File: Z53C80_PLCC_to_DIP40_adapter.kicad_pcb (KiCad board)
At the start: 4 copper layers, 21.8 x 51.1 mm, 2 parts, among them J1 DIP40, J2 PLCC44

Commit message: Update PCB
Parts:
- added C1: 100nF, Capacitor_SMD:C_1206_3216Metric_Pad1.33x1.80mm_HandSolder, B.Cu at (105.9, 81.5)
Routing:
- net GND: track 0.00 -> 145.7 mm, vias 0 -> 35
- net /~{DB3}: track 0.00 -> 33.9 mm
- net /~{DB6}: track 0.00 -> 31.9 mm
- net /~{DB7}: track 0.00 -> 31.9 mm
- net /~{CS}: track 0.00 -> 30.7 mm
- net /~{MSG}: track 0.00 -> 28.5 mm
- net /C/~{D}: track 0.00 -> 25.9 mm
- net /~{DB5}: track 0.00 -> 25.8 mm
- net /~{REQ}: track 0.00 -> 25.6 mm
- net /~{IOR}: track 0.00 -> 23.4 mm
- net /~{DB4}: track 0.00 -> 23.4 mm
- net /I/~{O}: track 0.00 -> 20.5 mm
- net /~{DB2}: track 0.00 -> 18.3 mm
- net /IRQ: track 0.00 -> 18.3 mm
- net /DRQ: track 0.00 -> 18.0 mm
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- added copper zone on B.Cu, net GND
- added copper zone on F.Cu, net GND
- added copper zone on In1.Cu, net GND
- added copper zone on In2.Cu, net GND

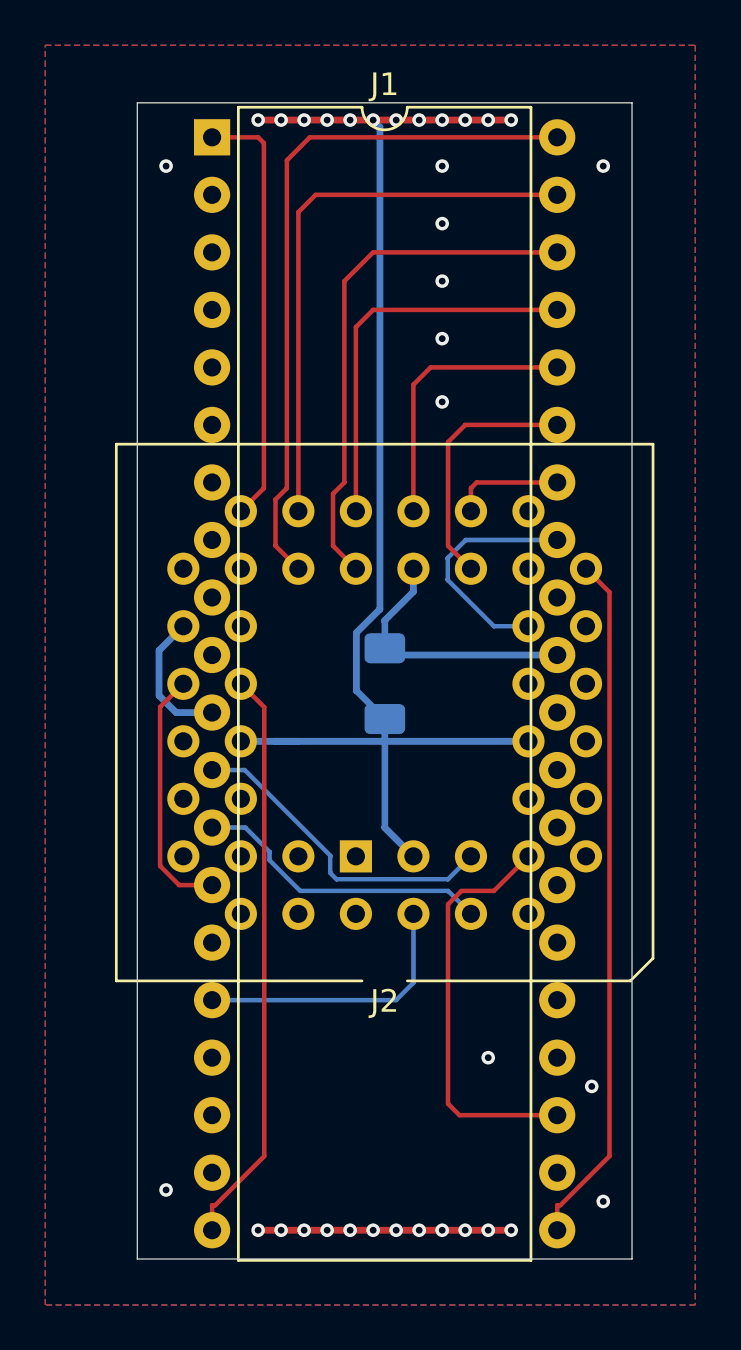
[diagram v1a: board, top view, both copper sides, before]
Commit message: Some more trace reorg
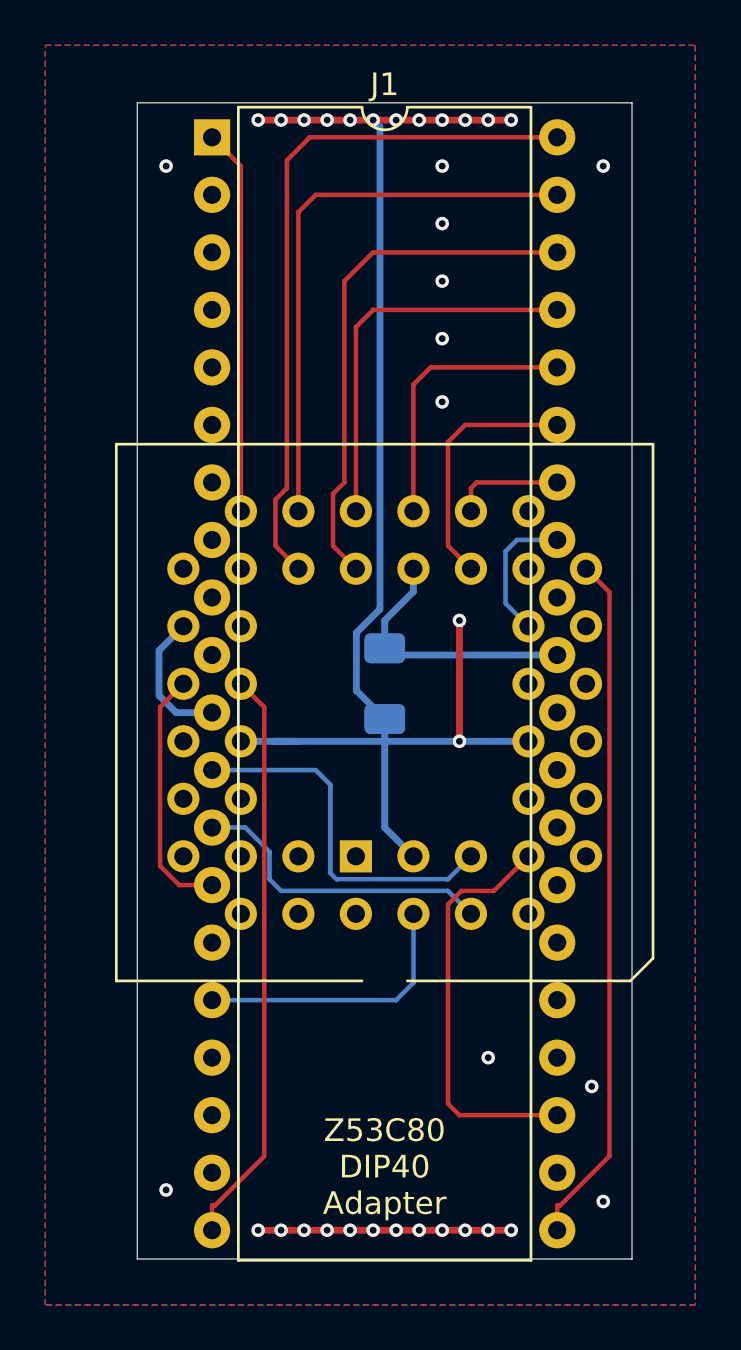
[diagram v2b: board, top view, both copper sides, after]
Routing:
- net GND: track 145.7 -> 151.0 mm, vias 35 -> 37
- net /A2: track 10.6 -> 6.22 mm
- net /D0: track 19.1 -> 17.0 mm
- net /~{SEL}: track 14.3 -> 16.1 mm
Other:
- board text added: "Z53C80 DIP40 Adapter"
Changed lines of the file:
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@@
 			(at -1.27 -6.4 0)
 			(layer "F.SilkS")
+			(hide yes)
 			(effects
 				(font
@@
 		(layer "Edge.Cuts")
 	)
-	(segment
-		(start 108.6996 75.9806)
-		(end 108.6996 76.9516)
+	(gr_text "Z53C80\nDIP40\nAdapter"
+		(at 105.918 102.87 0)
+		(layer "F.SilkS")
+		(effects
+			(font
+				(size 1 1)
+				(thickness 0.1)
+			)
+		)
+	)
+	(segment
+		(start 113.538 75.184)
+		(end 111.76 75.184)
 		(width 0.2)
 		(layer "B.Cu")
@@
 	)
 	(segment
-		(start 109.4962 75.184)
-		(end 108.6996 75.9806)
+		(start 111.2568 75.6872)
+		(end 111.76 75.184)
 		(width 0.2)
 		(layer "B.Cu")
@@
 	)
 	(segment
-		(start 108.6996 76.9516)
-		(end 110.742 78.994)
+		(start 111.2568 77.9828)
+		(end 111.2568 75.6872)
 		(width 0.2)
 		(layer "B.Cu")
@@
 	)
 	(segment
-		(start 110.742 78.994)
-		(end 112.268 78.994)
-		(width 0.2)
-		(layer "B.Cu")
-		(net 1)
-	)
-	(segment
-		(start 113.538 75.184)
-		(end 109.4962 75.184)
+		(start 112.268 78.994)
+		(end 111.2568 77.9828)
 		(width 0.2)
 		(layer "B.Cu")
@@
 	)
 	(segment
+		(start 100.838 88.9574)
+		(end 100.838 90.17)
+		(width 0.2)
+		(layer "B.Cu")
+		(net 10)
+	)
+	(segment
+		(start 99.7646 87.884)
+		(end 100.838 88.9574)
+		(width 0.2)
+		(layer "B.Cu")
+		(net 10)
+	)
+	(segment
 		(start 108.7131 90.6791)
-		(end 102.1894 90.6791)
+		(end 109.728 91.694)
 		(width 0.2)
 		(layer "B.Cu")
@@
 	)
 	(segment
-		(start 109.728 91.694)
+		(start 98.298 87.884)
+		(end 99.7646 87.884)
+		(width 0.2)
+		(layer "B.Cu")
+		(net 10)
+	)
+	(segment
+		(start 100.838 90.17)
+		(end 101.3471 90.6791)
+		(width 0.2)
+		(layer "B.Cu")
+		(net 10)
+	)
+	(segment
+		(start 101.3471 90.6791)
 		(end 108.7131 90.6791)
-		(width 0.2)
-		(layer "B.Cu")
-		(net 10)
-	)
-	(segment
-		(start 100.838 88.9574)
-		(end 99.7646 87.884)
-		(width 0.2)
-		(layer "B.Cu")
-		(net 10)
-	)
-	(segment
-		(start 102.1894 90.6791)
-		(end 100.838 89.3277)
-		(width 0.2)
-		(layer "B.Cu")
-		(net 10)
-	)
-	(segment
-		(start 100.838 89.3277)
-		(end 100.838 88.9574)
-		(width 0.2)
-		(layer "B.Cu")
-		(net 10)
-	)
-	(segment
-		(start 99.7646 87.884)
-		(end 98.298 87.884)
 		(width 0.2)
 		(layer "B.Cu")
@@
 	)
 	(segment
+		(start 102.87 85.344)
+		(end 98.298 85.344)
+		(width 0.2)
+		(layer "B.Cu")
+		(net 14)
+	)
+	(segment
+		(start 108.7151 90.1669)
+		(end 103.7956 90.1669)
+		(width 0.2)
+		(layer "B.Cu")
+		(net 14)
+	)
+	(segment
+		(start 103.5196 85.9936)
+		(end 102.87 85.344)
+		(width 0.2)
+		(layer "B.Cu")
+		(net 14)
+	)
+	(segment
+		(start 103.5196 89.8909)
+		(end 103.5196 85.9936)
+		(width 0.2)
+		(layer "B.Cu")
+		(net 14)
+	)
+	(segment
 		(start 103.7956 90.1669)
 		(end 103.5196 89.8909)
@@
 	)
 	(segment
-		(start 103.5196 89.1253)
-		(end 99.7383 85.344)
-		(width 0.2)
-		(layer "B.Cu")
-		(net 14)
-	)
-	(segment
-		(start 103.5196 89.8909)
-		(end 103.5196 89.1253)
-		(width 0.2)
-		(layer "B.Cu")
-		(net 14)
-	)
-	(segment
-		(start 99.7383 85.344)
-		(end 98.298 85.344)
-		(width 0.2)
-		(layer "B.Cu")
-		(net 14)
-	)
-	(segment
-		(start 108.7151 90.1669)
-		(end 103.7956 90.1669)
-		(width 0.2)
-		(layer "B.Cu")
-		(net 14)
+		(start 109.22 84.074)
+		(end 109.22 78.74)
+		(width 0.3)
+		(layer "F.Cu")
+		(net 15)
 	)
 	(segment
@@
 	)
 	(via
+		(at 109.22 78.74)
+		(size 0.6)
+		(drill 0.3)
+		(layers "F.Cu" "B.Cu")
+		(net 15)
+	)
+	(via
 		(at 101.346 105.664)
 		(size 0.6)
@@
 		(layers "F.Cu" "B.Cu")
 		(free yes)
+		(net 15)
+	)
+	(via
+		(at 109.22 84.074)
+		(size 0.6)
+		(drill 0.3)
+		(layers "F.Cu" "B.Cu")
 		(net 15)
 	)
@@
 	)
 	(segment
+		(start 112.268 84.074)
+		(end 105.923 84.074)
+		(width 0.3)
+		(layer "B.Cu")
+		(net 15)
+	)
+	(segment
 		(start 105.7092 56.9412)
 		(end 105.41 56.642)
@@
 	)
 	(segment
-		(start 112.268 84.074)
-		(end 105.923 84.074)
-		(width 0.3)
-		(layer "B.Cu")
-		(net 15)
-	)
-	(segment
 		(start 104.673 81.8415)
 		(end 104.673 79.277893)
@@
 	)
 	(segment
-		(start 100.584 72.898)
-		(end 100.584 57.658)
+		(start 99.568 73.914)
+		(end 99.568 58.674)
 		(width 0.2)
 		(layer "F.Cu")
@@
 	)
 	(segment
-		(start 100.584 57.658)
-		(end 100.33 57.404)
-		(width 0.2)
-		(layer "F.Cu")
-		(net 36)
-	)
-	(segment
-		(start 99.568 73.914)
-		(end 100.584 72.898)
-		(width 0.2)
-		(layer "F.Cu")
-		(net 36)
-	)
-	(segment
-		(start 100.33 57.404)
+		(start 99.568 58.674)
 		(end 98.298 57.404)
 		(width 0.2)

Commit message: Update PCB
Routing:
- net GND: track 151.0 -> 176.7 mm, vias 37 -> 63
- net /~{DB6}: track 31.9 -> 34.5 mm
- net /~{DB7}: track 31.9 -> 34.4 mm
- net /~{DB3}: track 33.9 -> 36.2 mm
- net /~{DB2}: track 18.3 -> 20.3 mm
- net /C/~{D}: track 25.9 -> 27.0 mm
- net /~{DB5}: track 25.8 -> 26.9 mm
- net /~{DB4}: track 23.4 -> 24.5 mm
- net /READY: track 15.8 -> 16.9 mm
- net /DRQ: track 18.0 -> 18.9 mm
- net /~{REQ}: track 25.6 -> 26.6 mm
- net /~{IOR}: track 23.4 -> 24.4 mm
- net /I/~{O}: track 20.5 -> 21.5 mm
- net /~{DACK}: track 10.4 -> 11.2 mm
- net /~{RESET}: track 2.44 -> 1.80 mm
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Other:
- outline, holes or cut-outs redrawn

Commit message: Remove spurious trace
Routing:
- net /~{DB2}: track 20.3 -> 18.2 mm
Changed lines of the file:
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@@
-	)
-	(segment
-		(start 95.5807 87.7067)
-		(end 97.028 89.154)
-		(width 0.2)
-		(layer "In1.Cu")
-		(net 9)
 	)
 	(segment

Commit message: Further adjustments to routing
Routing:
- net GND: track 176.7 -> 178.5 mm, vias 63 -> 65
- net /D3: track 23.3 -> 23.8 mm
- net VCC: vias 0 -> 1
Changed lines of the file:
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@@
 		)
+	)
+	(gr_line
+		(start 105.418 94.554)
+		(end 105.918 93.554)
+		(stroke
+			(width 0.1)
+			(type default)
+		)
+		(layer "F.SilkS")
+	)
+	(gr_line
+		(start 105.418 94.554)
+		(end 106.418 94.554)
+		(stroke
+			(width 0.1)
+			(type default)
+		)
+		(layer "F.SilkS")
+	)
+	(gr_line
+		(start 106.418 94.554)
+		(end 105.918 93.554)
+		(stroke
+			(width 0.1)
+			(type default)
+		)
+		(layer "F.SilkS")
 	)
 	(gr_arc
@@
 	)
 	(via
+		(at 109.982 71.374)
+		(size 0.6)
+		(drill 0.3)
+		(layers "F.Cu" "B.Cu")
+		(free yes)
+		(net 15)
+	)
+	(via
 		(at 96.266 64.77)
 		(size 0.6)
@@
 		(layers "F.Cu" "B.Cu")
 		(free yes)
+		(net 15)
+	)
+	(via
+		(at 105.90375 83.07225)
+		(size 0.6)
+		(drill 0.3)
+		(layers "F.Cu" "B.Cu")
 		(net 15)
 	)
@@
 	)
 	(segment
+		(start 108.458 69.088)
+		(end 108.458 70.866)
+		(width 0.3)
+		(layer "In1.Cu")
+		(net 15)
+	)
+	(segment
 		(start 115.45 104.514)
 		(end 115.57 104.394)
@@
 	)
 	(segment
+		(start 108.966 71.374)
+		(end 109.982 71.374)
+		(width 0.3)
+		(layer "In1.Cu")
+		(net 15)
+	)
+	(segment
 		(start 108.458 56.642)
 		(end 108.458 69.088)
@@
 	)
 	(segment
+		(start 108.458 70.866)
+		(end 108.966 71.374)
+		(width 0.3)
+		(layer "In1.Cu")
+		(net 15)
+	)
+	(segment
 		(start 112.656 104.514)
 		(end 115.45 104.514)
@@
 	)
 	(segment
-		(start 101.092 84.074)
-		(end 105.923 84.074)
-		(width 0.3)
-		(layer "B.Cu")
-		(net 15)
-	)
-	(segment
 		(start 105.923 83.0915)
 		(end 105.923 84.074)
@@
 	(segment
 		(start 105.923 83.0915)
-		(end 104.673 81.8415)
-		(width 0.3)
-		(layer "B.Cu")
-		(net 15)
-	)
-	(segment
-		(start 112.268 84.074)
-		(end 105.923 84.074)
+		(end 105.90375 83.07225)
+		(width 0.3)
+		(layer "B.Cu")
+		(net 15)
+	)
+	(segment
+		(start 109.22 84.074)
+		(end 108.204 84.074)
+		(width 0.3)
+		(layer "B.Cu")
+		(net 15)
+	)
+	(segment
+		(start 108.204 84.074)
+		(end 107.188 85.09)
+		(width 0.3)
+		(layer "B.Cu")
+		(net 15)
+	)
+	(segment
+		(start 98.298 82.804)
+		(end 96.712 82.804)
+		(width 0.3)
+		(layer "B.Cu")
+		(net 15)
+	)
+	(segment
+		(start 104.902 85.09)
+		(end 105.664 85.09)
+		(width 0.3)
+		(layer "B.Cu")
+		(net 15)
+	)
+	(segment
+		(start 105.7092 77.4248)
+		(end 105.7092 56.9412)
+		(width 0.3)
+		(layer "B.Cu")
+		(net 15)
+	)
+	(segment
+		(start 103.886 84.074)
+		(end 104.902 85.09)
+		(width 0.3)
+		(layer "B.Cu")
+		(net 15)
+	)
+	(segment
+		(start 103.886 78.74)
+		(end 104.14 78.486)
 		(width 0.3)
 		(layer "B.Cu")
@@
 	)
 	(segment
-		(start 101.092 84.074)
-		(end 102.108 84.074)
-		(width 0.3)
-		(layer "B.Cu")
-		(net 15)
-	)
-	(segment
-		(start 105.7092 78.241693)
-		(end 105.7092 56.9412)
-		(width 0.3)
-		(layer "B.Cu")
-		(net 15)
-	)
-	(segment
-		(start 98.298 82.804)
-		(end 96.712 82.804)
-		(width 0.3)
-		(layer "B.Cu")
-		(net 15)
-	)
-	(segment
-		(start 99.568 84.074)
-		(end 101.092 84.074)
-		(width 0.3)
-		(layer "B.Cu")
-		(net 15)
-	)
-	(segment
-		(start 104.673 81.8415)
-		(end 104.673 79.277893)
+		(start 104.40825 82.05625)
+		(end 103.886 81.534)
+		(width 0.3)
+		(layer "B.Cu")
+		(net 15)
+	)
+	(segment
+		(start 103.886 81.534)
+		(end 103.886 78.74)
 		(width 0.3)
 		(layer "B.Cu")
@@
 	)
 	(segment
+		(start 99.568 84.074)
+		(end 103.886 84.074)
+		(width 0.3)
+		(layer "B.Cu")
+		(net 15)
+	)
+	(segment
+		(start 104.88775 82.05625)
+		(end 104.40825 82.05625)
+		(width 0.3)
+		(layer "B.Cu")
+		(net 15)
+	)
+	(segment
+		(start 105.664 85.09)
+		(end 105.923 85.09)
+		(width 0.3)
+		(layer "B.Cu")
+		(net 15)
+	)
+	(segment
 		(start 95.9559 80.0661)
 		(end 97.028 78.994)
@@
 	)
 	(segment
+		(start 107.188 85.09)
+		(end 105.664 85.09)
+		(width 0.3)
+		(layer "B.Cu")
+		(net 15)
+	)
+	(segment
 		(start 96.712 82.804)
 		(end 95.9559 82.0479)
@@
 	(segment
 		(start 105.923 84.074)
+		(end 105.923 85.09)
+		(width 0.3)
+		(layer "B.Cu")
+		(net 15)
+	)
+	(segment
+		(start 105.90375 83.07225)
+		(end 104.88775 82.05625)
+		(width 0.3)
+		(layer "B.Cu")
+		(net 15)
+	)
+	(segment
+		(start 105.923 85.09)
 		(end 105.923 87.889)
-		(width 0.3)
-		(layer "B.Cu")
-		(net 15)
-	)
-	(segment
-		(start 104.673 79.277893)
-		(end 105.7092 78.241693)
 		(width 0.3)
 		(layer "B.Cu")
@@
 	)
 	(segment
+		(start 104.648 78.486)
+		(end 105.7092 77.4248)
+		(width 0.3)
+		(layer "B.Cu")
+		(net 15)
+	)
+	(segment
+		(start 104.14 78.486)
+		(end 104.648 78.486)
+		(width 0.3)
+		(layer "B.Cu")
+		(net 15)
+	)
+	(segment
 		(start 102.108 73.914)
 		(end 102.108 60.706)
@@
 		(net 18)
 	)
+	(via
+		(at 105.94225 79.98575)
+		(size 0.6)
+		(drill 0.3)
+		(layers "F.Cu" "B.Cu")
+		(net 19)
+	)
 	(segment
 		(start 105.923 78.735)
@@
 	)
 	(segment
+		(start 105.94225 79.98575)
+		(end 105.923 79.9665)
+		(width 0.3)
+		(layer "B.Cu")
+		(net 19)
+	)
+	(segment
 		(start 113.538 80.264)
 		(end 106.2205 80.264)
@@
 	(segment
 		(start 106.2205 80.264)
-		(end 105.923 79.9665)
+		(end 105.94225 79.98575)
 		(width 0.3)
 		(layer "B.Cu")
@@
 	)
 	(segment
-		(start 104.14 72.644)
-		(end 104.14 63.754)
+		(start 103.637 63.246)
+		(end 103.637 75.4428)
 		(width 0.2)
 		(layer "F.Cu")
@@
 	(segment
 		(start 103.637 75.4428)
-		(end 103.637 73.1472)
+		(end 104.648 76.454)
 		(width 0.2)
 		(layer "F.Cu")
@@
 	)
 	(segment
-		(start 104.648 76.454)
-		(end 103.637 75.4428)
+		(start 113.538 62.484)
+		(end 104.399 62.484)
 		(width 0.2)
 		(layer "F.Cu")
@@
 	)
 	(segment
-		(start 105.41 62.484)
-		(end 113.538 62.484)
-		(width 0.2)
-		(layer "F.Cu")
-		(net 23)
-	)
-	(segment
-		(start 104.14 63.754)
-		(end 105.41 62.484)
-		(width 0.2)
-		(layer "F.Cu")
-		(net 23)
-	)
-	(segment
-		(start 103.637 73.1472)
-		(end 104.14 72.644)
-		(width 0.2)
-		(layer "F.Cu")
+		(start 104.399 62.484)
+		(end 103.637 63.246)
+		(width 0.2)
+		(layer "F.Cu")

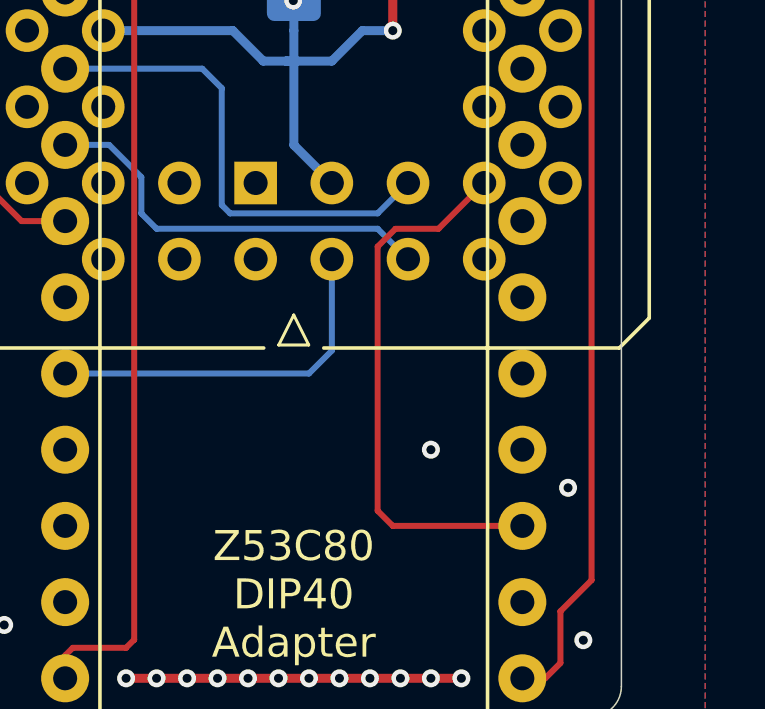
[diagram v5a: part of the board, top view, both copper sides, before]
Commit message: Further routing changes
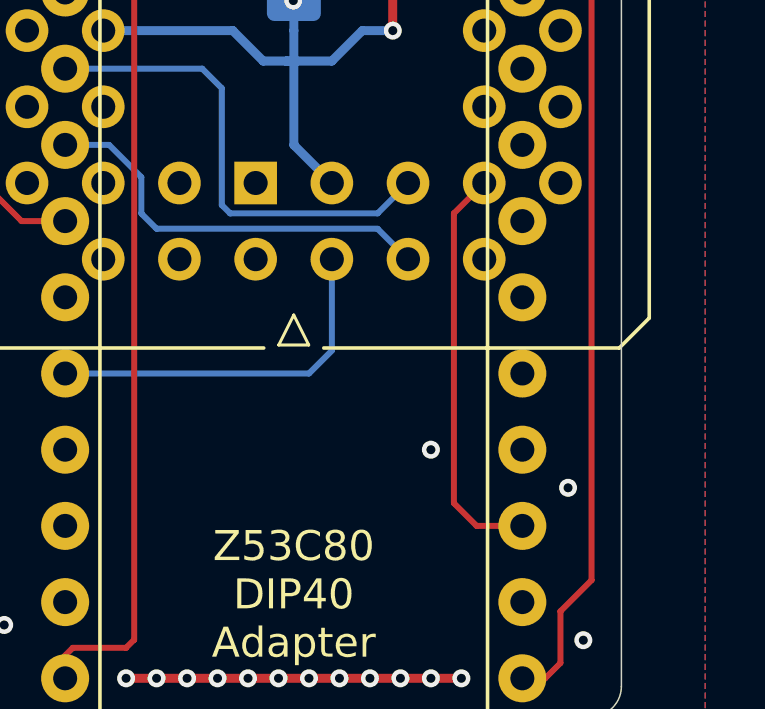
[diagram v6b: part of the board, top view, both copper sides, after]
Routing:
- net /IRQ: track 18.3 -> 13.7 mm
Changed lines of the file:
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@@
 			(outputformat 1)
 			(mirror no)
-			(drillshape 1)
+			(drillshape 0)
 			(scaleselection 1)
-			(outputdirectory "")
+			(outputdirectory "gerbers/")
 		)
 	)
@@
 	)
 	(segment
-		(start 108.7151 100.0791)
-		(end 109.22 100.584)
-		(width 0.2)
-		(layer "F.Cu")
-		(net 25)
-	)
-	(segment
-		(start 110.7409 90.6811)
-		(end 109.3085 90.6811)
-		(width 0.2)
-		(layer "F.Cu")
-		(net 25)
-	)
-	(segment
-		(start 109.3085 90.6811)
-		(end 108.7151 91.2745)
+		(start 112.014 100.584)
+		(end 113.538 100.584)
 		(width 0.2)
 		(layer "F.Cu")
@@
 	)
 	(segment
-		(start 108.7151 91.2745)
-		(end 108.7151 100.0791)
+		(start 111.2568 90.1652)
+		(end 111.2568 99.8268)
 		(width 0.2)
 		(layer "F.Cu")
@@
 	(segment
 		(start 112.268 89.154)
-		(end 110.7409 90.6811)
+		(end 111.2568 90.1652)
 		(width 0.2)
 		(layer "F.Cu")
@@
 	)
 	(segment
-		(start 109.22 100.584)
-		(end 113.538 100.584)
+		(start 111.2568 99.8268)
+		(end 112.014 100.584)
 		(width 0.2)
 		(layer "F.Cu")
